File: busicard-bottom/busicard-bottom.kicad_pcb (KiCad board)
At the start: 2 copper layers, 70 x 46 mm, 12 parts, among them SW1 SW_Push

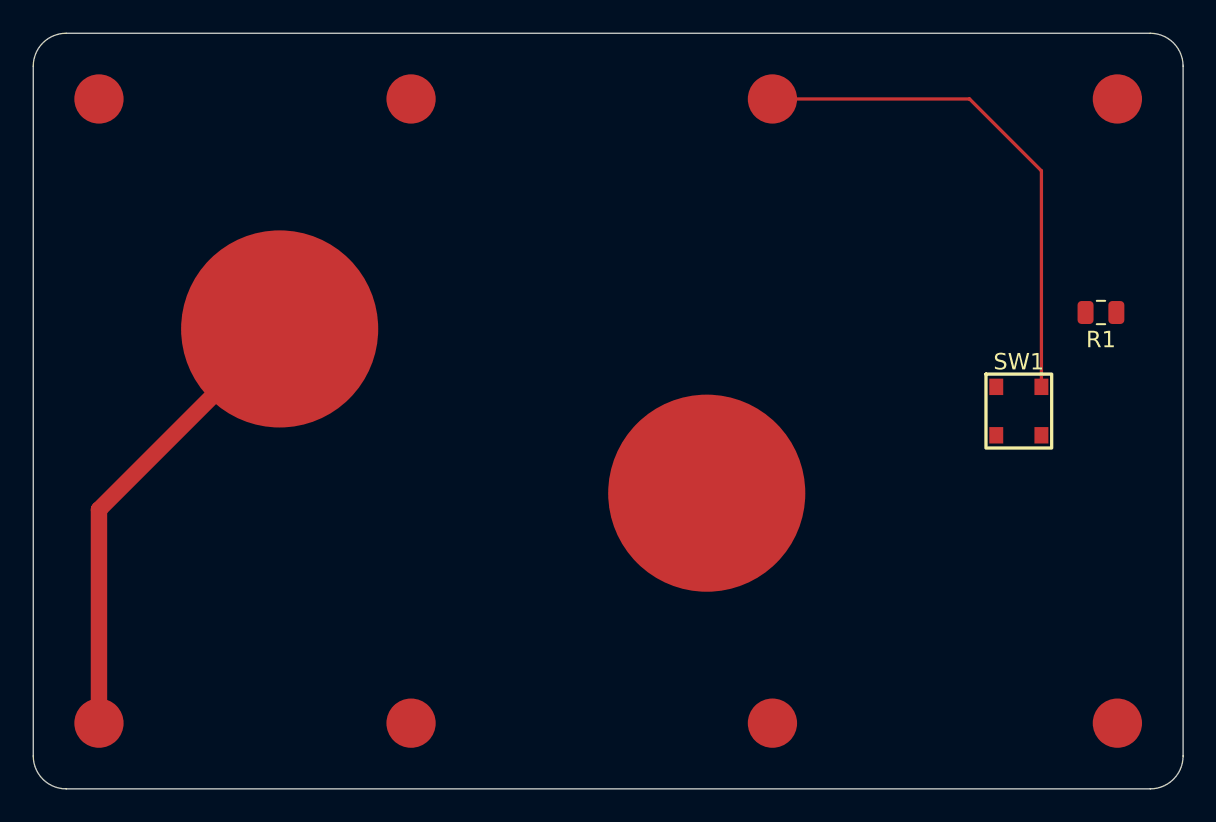
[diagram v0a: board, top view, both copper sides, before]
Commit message: First pass at ready for production
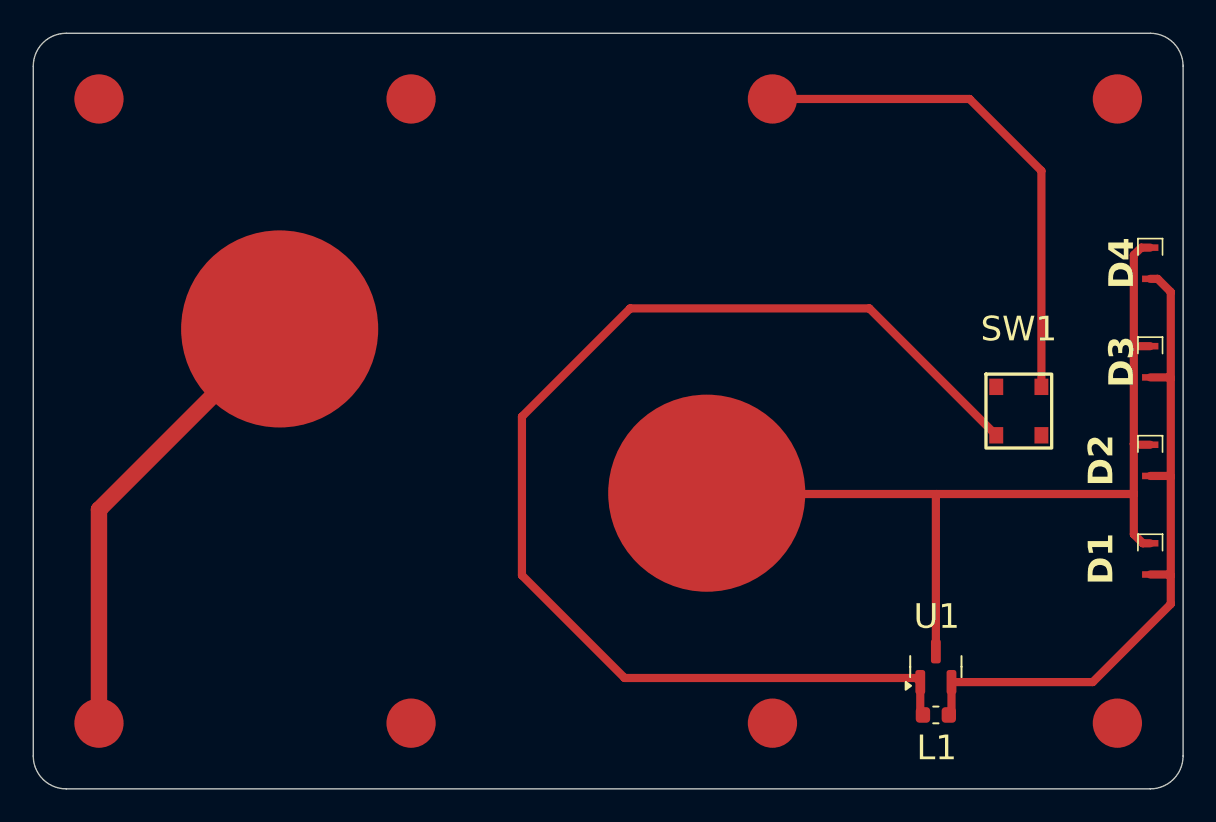
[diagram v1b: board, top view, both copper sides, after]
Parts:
- removed R1: R, lib:R_0805_2012Metric
- added D1: LED, lib:JLCPCB_SIDE_C409529, F.Cu at (198.0, 109.0)
- added D2: LED, lib:JLCPCB_SIDE_C409529, F.Cu at (198.0, 103.0)
- added D3: LED, lib:JLCPCB_SIDE_C409529, F.Cu at (198.0, 97.0)
- added D4: LED, lib:JLCPCB_SIDE_C409529, F.Cu at (198.0, 91.0)
- added L1: 22uH, lib:L_0603_1608Metric, F.Cu at (184.9, 118.5)
- added U1: ZXSC380FHTA, lib:SOT-23, F.Cu at (184.9, 115.6)
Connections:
- TP3 pad 1: /BATT2- -> GND
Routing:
- net Net-(U1-VCC): track 0.00 -> 73.2 mm
- net GND: track 0.00 -> 57.0 mm
- net Net-(D1-A): track 0.00 -> 41.5 mm

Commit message: More steps to production
- add slik
- add paste to battery pads
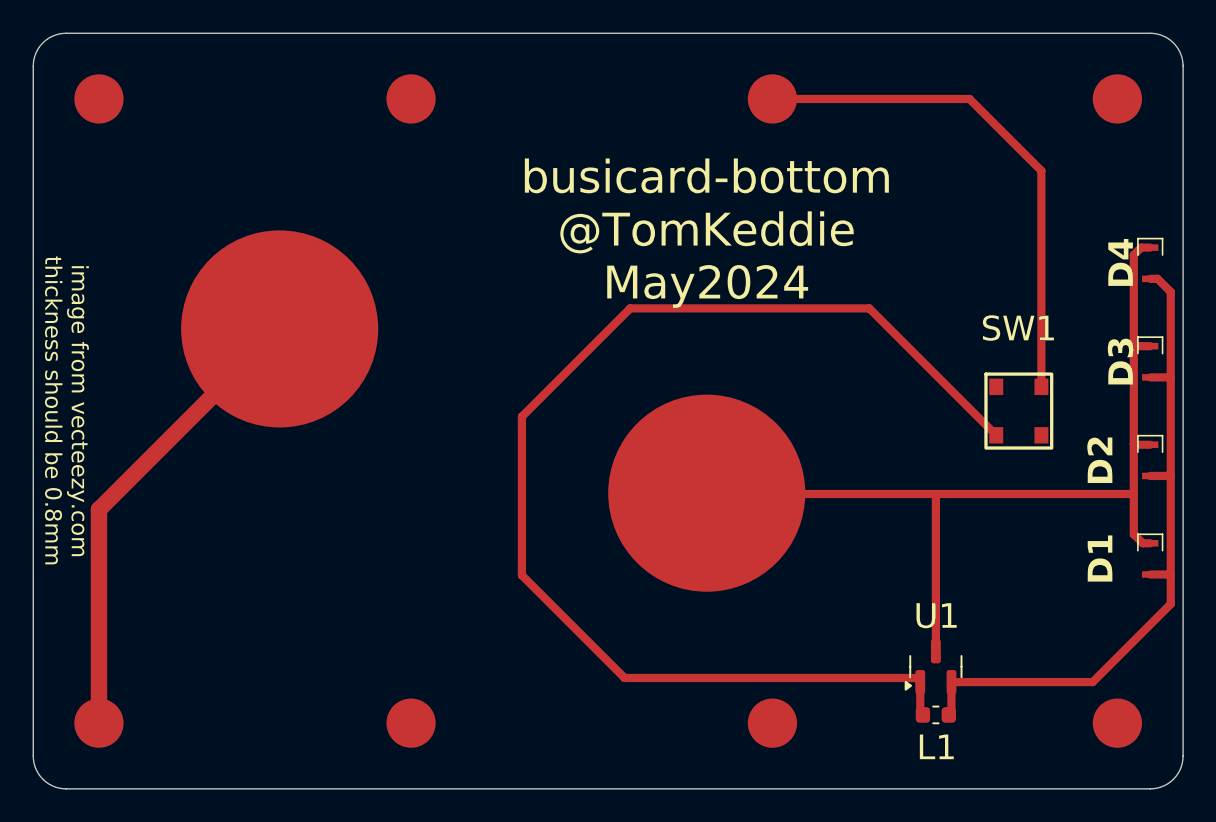
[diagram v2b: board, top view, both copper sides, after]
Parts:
- added G***: LOGO, lib:flashlight, B.Cu at (164.6, 101.2)
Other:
- board text added: "busicard-bottom @TomKeddie May2024"
- board text added: "image from vecteezy.com thickness should be 0.8mm"

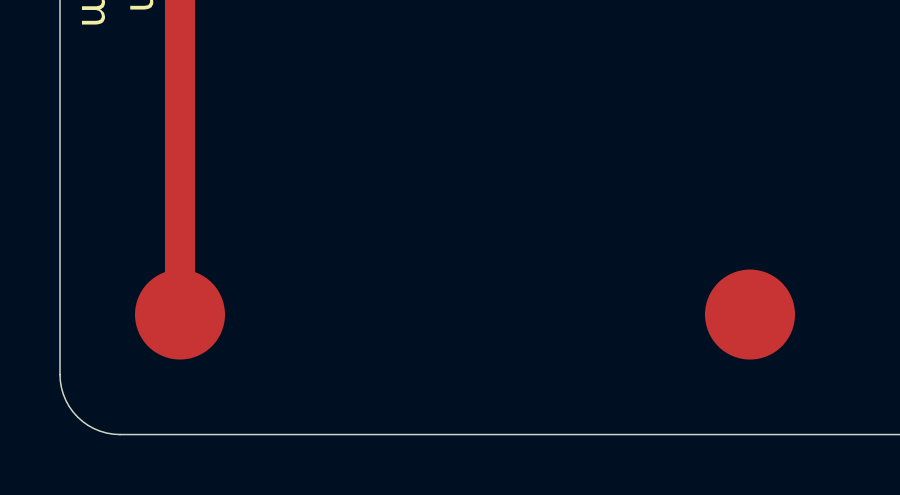
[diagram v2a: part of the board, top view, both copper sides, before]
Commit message: Add assembly holes and batch number on silkscreen
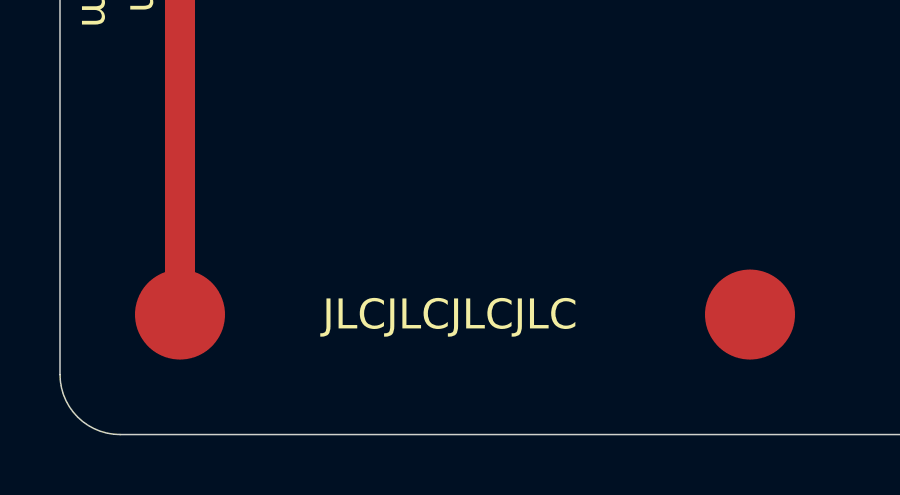
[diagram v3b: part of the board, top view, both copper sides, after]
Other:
- board text added: "JLCJLCJLCJLC"
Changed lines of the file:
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@@
 		(fp_poly
 			(pts
-				(xy -4.533258 0.021923) (xy -4.239059 0.016993) (xy -4.004719 0.007918) (xy -3.820638 -0.006092)
+				(xy -4.533259 0.021923) (xy -4.239059 0.016993) (xy -4.004719 0.007918) (xy -3.820638 -0.006092)
 				(xy -3.677217 -0.025825) (xy -3.564855 -0.052072) (xy -3.473956 -0.085621) (xy -3.394918 -0.127262)
 				(xy -3.318144 -0.177783) (xy -3.298349 -0.191772) (xy -3.153214 -0.341507) (xy -3.02556 -0.556742)
@@
 				(xy -13.375499 -0.045969) (xy -13.207317 -0.038742) (xy -12.960194 -0.031718) (xy -12.643789 -0.025066)
 				(xy -12.267759 -0.018952) (xy -11.841765 -0.013542) (xy -11.375465 -0.009003) (xy -10.878517 -0.005502)
-				(xy -10.611993 -0.004151) (xy -10.017189 -0.001472) (xy -9.378273 0.001523) (xy -8.716156 0.004727)
+				(xy -10.611993 -0.004151) (xy -10.017189 -0.001472) (xy -9.378273 0.001523) (xy -8.716157 0.004727)
 				(xy -8.051746 0.008036) (xy -7.405955 0.011344) (xy -6.799692 0.014546) (xy -6.253868 0.017537)
 				(xy -5.870987 0.019729) (xy -5.339621 0.022502) (xy -4.896911 0.023496)
@@
 				(xy -32.478838 0.825061) (xy -32.484119 1.891489) (xy -32.486466 2.469681) (xy -32.486932 2.958036)
 				(xy -32.484974 3.364967) (xy -32.480049 3.698886) (xy -32.471613 3.968208) (xy -32.459123 4.181344)
-				(xy -32.442034 4.346708) (xy -32.419805 4.472712) (xy -32.391891 4.567771) (xy -32.357748 4.640296)
+				(xy -32.442034 4.346708) (xy -32.419805 4.472712) (xy -32.391891 4.567771) (xy -32.357747 4.640296)
 				(xy -32.316836 4.698701) (xy -32.301639 4.716441) (xy -32.251434 4.790399) (xy -32.244797 4.82079)
 				(xy -32.221199 4.884711) (xy -32.142589 4.995561) (xy -32.026457 5.133951) (xy -31.890293 5.280489)
@@
 				(xy 32.514689 -0.762389) (xy 32.522681 -1.356827) (xy 32.529045 -1.965424) (xy 32.53373 -2.57713)
 				(xy 32.536685 -3.180896) (xy 32.537857 -3.765674) (xy 32.537197 -4.320414) (xy 32.534651 -4.834068)
-				(xy 32.53017 -5.295587) (xy 32.523701 -5.693922) (xy 32.515194 -6.018022) (xy 32.504596 -6.256843)
+				(xy 32.53017 -5.295587) (xy 32.523701 -5.693922) (xy 32.515194 -6.018021) (xy 32.504596 -6.256843)
 				(xy 32.502554 -6.288588) (xy 32.491546 -6.465577) (xy 32.477958 -6.708125) (xy 32.463552 -6.983628)
 				(xy 32.450698 -7.246616) (xy 32.437581 -7.502638) (xy 32.423602 -7.736714) (xy 32.410374 -7.92404)
@@
 				(xy 7.035548 5.895402) (xy 7.039206 5.731801) (xy 7.042937 5.485136) (xy 7.046717 5.162097) (xy 7.050519 4.769379)
 				(xy 7.05432 4.313673) (xy 7.058096 3.801673) (xy 7.06182 3.240069) (xy 7.065469 2.635555) (xy 7.069018 1.994824)
-				(xy 7.072442 1.324567) (xy 7.075716 0.631478) (xy 7.078815 -0.077752) (xy 7.081716 -0.796429) (xy 7.084392 -1.517861)
+				(xy 7.072442 1.324567) (xy 7.075716 0.631478) (xy 7.078815 -0.077752) (xy 7.081716 -0.796429) (xy 7.084392 -1.51786)
 				(xy 7.08682 -2.235358) (xy 7.088975 -2.942224) (xy 7.090832 -3.631769) (xy 7.092366 -4.297299) (xy 7.093552 -4.932122)
 				(xy 7.094366 -5.529545) (xy 7.094783 -6.082877) (xy 7.094778 -6.585424) (xy 7.094327 -7.030495)
@@
 		(layer "Edge.Cuts")
 	)
+	(gr_text "JLCJLCJLCJLC"
+		(at 143 119 0)
+		(layer "F.SilkS")
+		(effects
+			(font
+				(size 1 1)
+				(thickness 0.1)
+			)
+		)
+	)
 	(gr_text "busicard-bottom\n@TomKeddie\nMay2024"
